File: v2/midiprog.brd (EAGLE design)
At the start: 99.1 x 78.7 mm, 56 parts, among them IC1 PIC18F4550_40, IC2 TPIC6B596N, IC4 TPIC6B596N, Q2 2N2222A, Q3 2N2222A, Q4 2N2222A, Q5 8MHz

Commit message: Removed last via.
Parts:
- moved R5 3.81 mm to (49.5, 39.4)
- moved C8 2.84 mm to (31.8, 45.7)
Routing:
- net VDD: track 286.7 -> 293.5 mm
- net BTN_S0: track 71.1 -> 67.4 mm, vias 1 -> 0
- net SHIFTREG_SCL: track 59.7 -> 62.0 mm
- net N$16: track 15.9 -> 13.8 mm
- net BTN_S3: track 62.3 -> 63.0 mm
- net N$1: track 11.5 -> 12.3 mm
- net BTN_S1: track 68.1 -> 67.4 mm

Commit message: Reorg
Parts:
- moved R5 1.80 mm to (50.8, 40.6)
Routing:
- net VDD: track 293.5 -> 296.9 mm
- net N$17: track 11.5 -> 13.0 mm
- net BTN_IN: track 63.5 -> 64.5 mm
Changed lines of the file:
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@@
 <element name="PWR_CN" library="con-amp-quick" package="02P" value="" x="90.17" y="5.08" rot="R180"/>
 <element name="C9" library="rcl" package="C050-025X075" value=".1" x="7.62" y="44.45" rot="R180"/>
-<element name="R5" library="rcl" package="0207/10" value="10k" x="49.53" y="39.37" rot="R180"/>
+<element name="R5" library="rcl" package="0207/10" value="10k" x="50.8" y="40.64" rot="R180"/>
 <element name="D2" library="diode" package="DO41-10" value="1N4001" x="80.01" y="5.08"/>
 <element name="PWR_SW" library="con-amp-quick" package="02P" value="" x="69.85" y="5.08" rot="R180"/>
@@
 <wire x1="58.42" y1="10.16" x2="58.42" y2="34.29" width="0.4064" layer="1"/>
 <wire x1="58.42" y1="34.29" x2="63.5" y2="34.29" width="0.4064" layer="1"/>
-<wire x1="88.9" y1="29.21" x2="82.55" y2="35.56" width="0.4064" layer="1"/>
-<wire x1="82.55" y1="35.56" x2="78.74" y2="39.37" width="0.4064" layer="1"/>
+<wire x1="88.9" y1="29.21" x2="88.9" y2="31.75" width="0.4064" layer="1"/>
+<wire x1="88.9" y1="31.75" x2="87.63" y2="33.02" width="0.4064" layer="1"/>
+<wire x1="87.63" y1="33.02" x2="83.82" y2="33.02" width="0.4064" layer="1"/>
+<wire x1="83.82" y1="33.02" x2="82.55" y2="34.29" width="0.4064" layer="1"/>
+<wire x1="82.55" y1="34.29" x2="82.55" y2="35.56" width="0.4064" layer="1"/>
+<wire x1="82.55" y1="35.56" x2="82.55" y2="36.83" width="0.4064" layer="1"/>
+<wire x1="82.55" y1="36.83" x2="80.01" y2="39.37" width="0.4064" layer="1"/>
+<wire x1="80.01" y1="39.37" x2="78.74" y2="39.37" width="0.4064" layer="1"/>
 <wire x1="68.58" y1="64.77" x2="67.31" y2="66.04" width="0.4064" layer="1"/>
 <wire x1="67.31" y1="66.04" x2="67.31" y2="68.58" width="0.4064" layer="1"/>
@@
 <wire x1="63.5" y1="74.93" x2="60.96" y2="74.93" width="0.4064" layer="1"/>
 <wire x1="57.15" y1="74.93" x2="60.96" y2="74.93" width="0.4064" layer="1"/>
-<wire x1="44.45" y1="39.37" x2="48.26" y2="35.56" width="0.4064" layer="1"/>
+<wire x1="45.72" y1="40.64" x2="45.72" y2="38.1" width="0.4064" layer="1"/>
+<wire x1="45.72" y1="38.1" x2="48.26" y2="35.56" width="0.4064" layer="1"/>
 <wire x1="58.42" y1="35.56" x2="48.26" y2="35.56" width="0.4064" layer="1"/>
 <wire x1="58.42" y1="34.29" x2="58.42" y2="35.56" width="0.4064" layer="1"/>
@@
 <wire x1="10.16" y1="38.1" x2="16.51" y2="31.75" width="0.4064" layer="1"/>
 <wire x1="10.16" y1="44.45" x2="10.16" y2="38.1" width="0.4064" layer="1"/>
-<wire x1="68.58" y1="49.53" x2="78.74" y2="39.37" width="0.4064" layer="1"/>
-<wire x1="68.58" y1="64.77" x2="68.58" y2="49.53" width="0.4064" layer="1"/>
+<wire x1="68.58" y1="46.99" x2="76.2" y2="39.37" width="0.4064" layer="1"/>
+<wire x1="76.2" y1="39.37" x2="78.74" y2="39.37" width="0.4064" layer="1"/>
+<wire x1="68.58" y1="64.77" x2="68.58" y2="46.99" width="0.4064" layer="1"/>
 <wire x1="10.16" y1="44.45" x2="33.02" y2="44.45" width="0.4064" layer="1"/>
 <wire x1="33.02" y1="44.45" x2="34.29" y2="45.72" width="0.4064" layer="1"/>
 <wire x1="49.53" y1="44.45" x2="49.53" y2="49.53" width="0.4064" layer="16"/>
-<wire x1="44.45" y1="39.37" x2="49.53" y2="44.45" width="0.4064" layer="16"/>
+<wire x1="45.72" y1="40.64" x2="49.53" y2="44.45" width="0.4064" layer="16"/>
 <wire x1="20.32" y1="49.53" x2="20.32" y2="48.26" width="0.4064" layer="1"/>
 <wire x1="20.32" y1="48.26" x2="19.05" y2="46.99" width="0.4064" layer="1"/>
@@
 <contactref element="R5" pad="1"/>
 <contactref element="U$2" pad="3"/>
-<wire x1="63.5" y1="39.37" x2="54.61" y2="39.37" width="0.254" layer="1"/>
-<wire x1="50.8" y1="39.37" x2="54.61" y2="39.37" width="0.254" layer="16"/>
-<wire x1="41.91" y1="36.83" x2="48.26" y2="36.83" width="0.254" layer="16"/>
-<wire x1="48.26" y1="36.83" x2="50.8" y2="39.37" width="0.254" layer="16"/>
-<wire x1="34.29" y1="29.21" x2="41.91" y2="36.83" width="0.254" layer="16"/>
+<wire x1="63.5" y1="39.37" x2="57.15" y2="39.37" width="0.254" layer="1"/>
+<wire x1="57.15" y1="39.37" x2="55.88" y2="40.64" width="0.254" layer="1"/>
+<wire x1="52.07" y1="40.64" x2="55.88" y2="40.64" width="0.254" layer="16"/>
+<wire x1="43.18" y1="38.1" x2="49.53" y2="38.1" width="0.254" layer="16"/>
+<wire x1="49.53" y1="38.1" x2="52.07" y2="40.64" width="0.254" layer="16"/>
+<wire x1="34.29" y1="29.21" x2="43.18" y2="38.1" width="0.254" layer="16"/>
 <wire x1="34.29" y1="26.67" x2="34.29" y2="29.21" width="0.254" layer="16"/>
 <wire x1="31.75" y1="24.13" x2="34.29" y2="26.67" width="0.254" layer="16"/>
@@
 <contactref element="IC1" pad="40"/>
 <contactref element="ICD" pad="4"/>
-<wire x1="72.39" y1="68.58" x2="72.39" y2="66.04" width="0.4064" layer="1"/>
-<wire x1="72.39" y1="66.04" x2="78.74" y2="59.69" width="0.4064" layer="1"/>
+<wire x1="72.39" y1="68.58" x2="72.39" y2="63.5" width="0.4064" layer="1"/>
+<wire x1="72.39" y1="63.5" x2="76.2" y2="59.69" width="0.4064" layer="1"/>
+<wire x1="76.2" y1="59.69" x2="78.74" y2="59.69" width="0.4064" layer="1"/>
 </signal>
 <signal name="N$18">

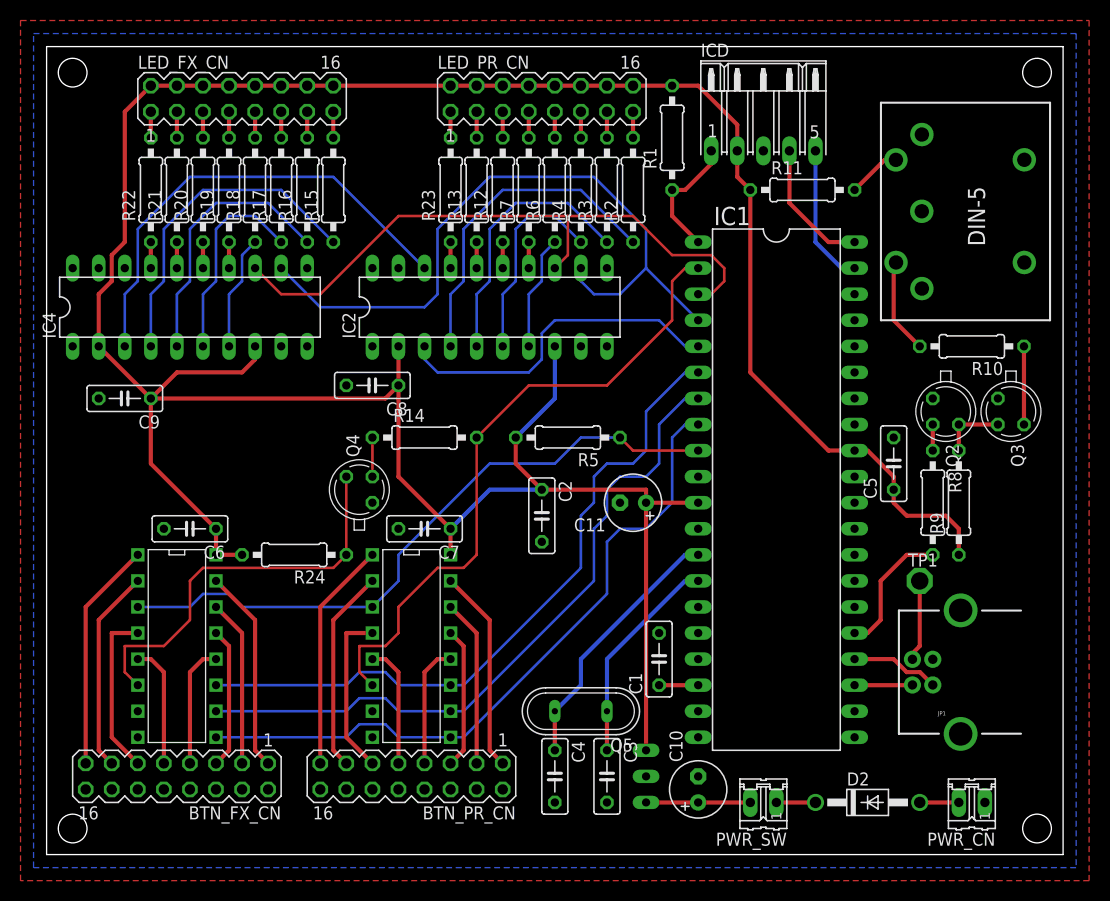
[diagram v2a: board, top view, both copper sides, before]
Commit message: More clearance between button headers and mux chips. Moved timing crystal closer to PIC. Swapped C11 and C2 positions. Swapped MIDI OUT pins.
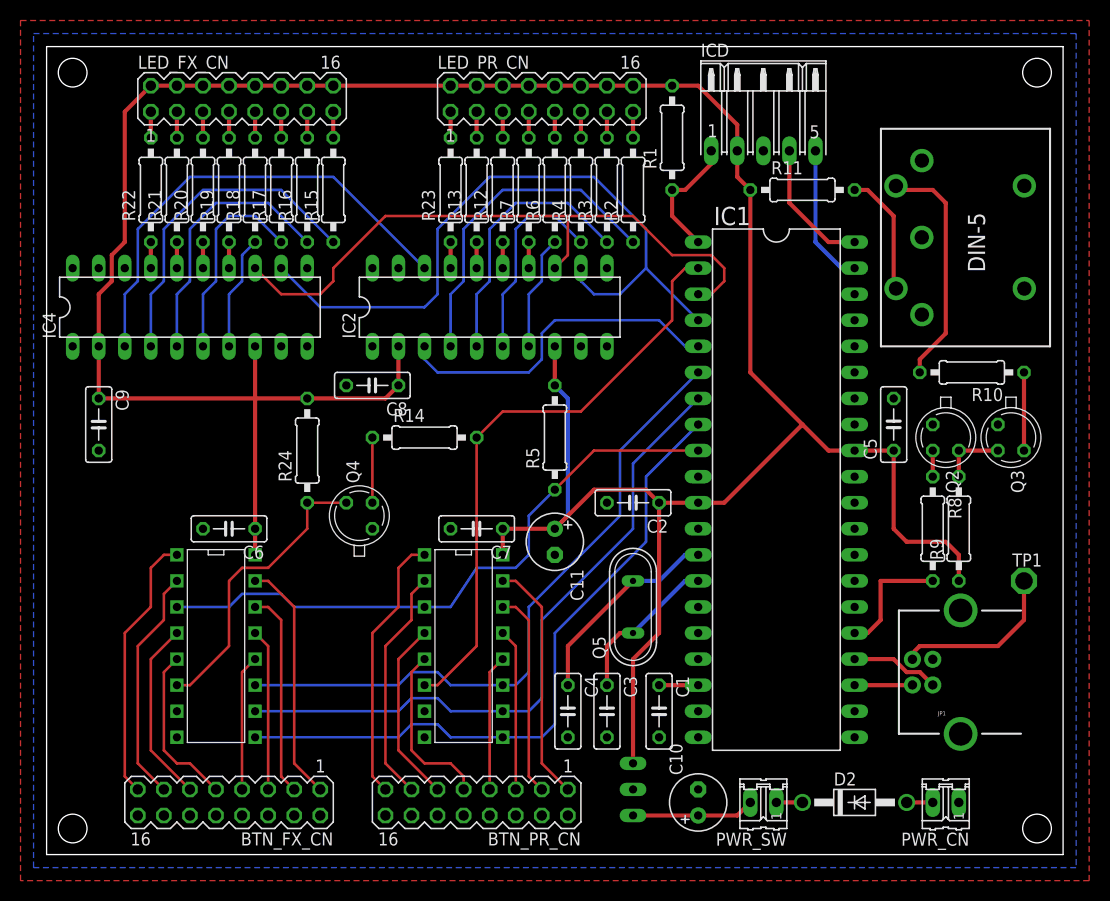
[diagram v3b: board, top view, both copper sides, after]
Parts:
- moved Q5 11.4 mm to (57.1, 24.1), turned to 90 degrees
- moved R24 10.2 mm to (25.4, 39.4), turned to 90 degrees
- moved TP1 10.2 mm to (95.2, 26.7)
- moved C2 8.98 mm to (57.1, 34.3), turned to 180 degrees
- moved C11 8.52 mm to (49.5, 30.5), turned to 270 degrees
- moved BTN_PR_CN 6.84 mm to (41.9, 5.08)
- moved C4 6.48 mm to (50.8, 14.0)
- moved C3 6.35 mm to (54.6, 14.0)
- moved BTN_FX_CN 5.68 mm to (17.8, 5.08)
- moved U$1 5.08 mm to (44.5, 19.1)
- moved C1 5.08 mm to (59.7, 14.0), turned to 270 degrees
- moved C7 5.08 mm to (41.9, 31.8)
- moved C6 3.81 mm to (17.8, 31.8)
- moved U$2 3.81 mm to (20.3, 19.1)
- moved C5 3.81 mm to (82.5, 41.9)
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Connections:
- net N$8: now also R11.2; no longer R10.2
- net N$9: now also R10.2; no longer R11.2
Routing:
- net N$9: track 5.24 -> 23.1 mm
- net N$54: track 39.5 -> 29.1 mm
- net VDD: track 296.9 -> 286.8 mm
- net USB_VCC: track 7.93 -> 16.6 mm
- net OSC2: track 20.9 -> 15.3 mm
- net OSC1: track 25.6 -> 20.2 mm
- net BTN_S3: track 63.0 -> 57.6 mm
- net N$47: track 12.0 -> 16.8 mm
- net N$46: track 12.0 -> 16.1 mm
- net N$64: track 19.9 -> 23.7 mm
- net N$52: track 22.4 -> 26.2 mm
- net N$63: track 16.3 -> 20.1 mm
- net N$60: track 22.4 -> 26.2 mm
- net N$57: track 16.3 -> 20.1 mm
- net N$58: track 19.9 -> 23.7 mm
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
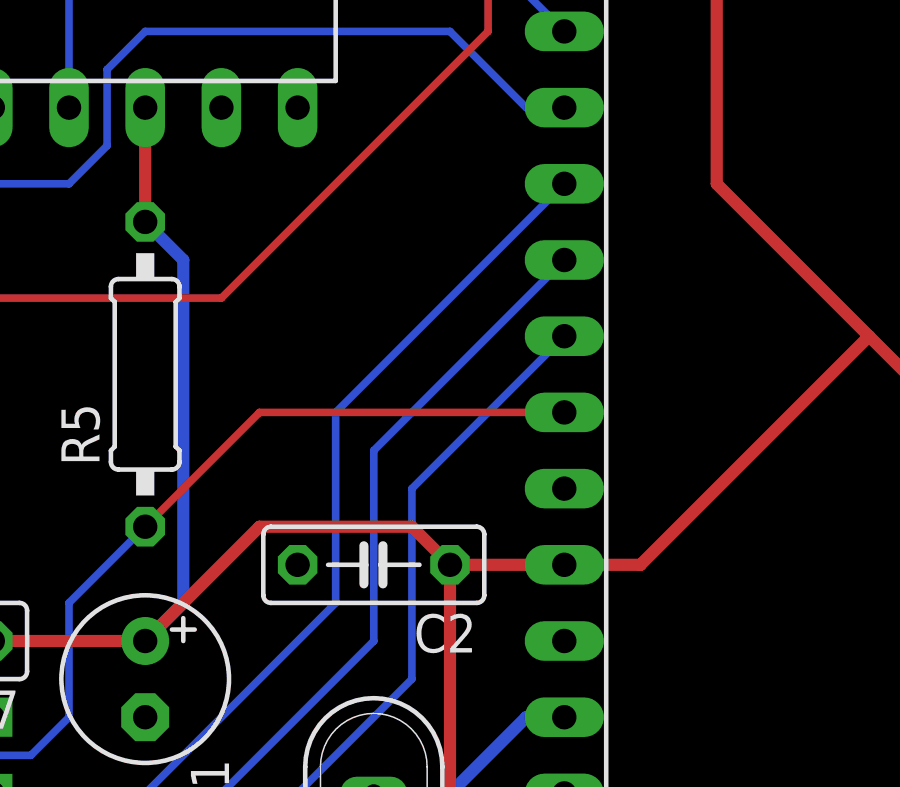
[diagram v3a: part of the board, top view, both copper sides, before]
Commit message: Fixed missing chunk of bottom ground plane.
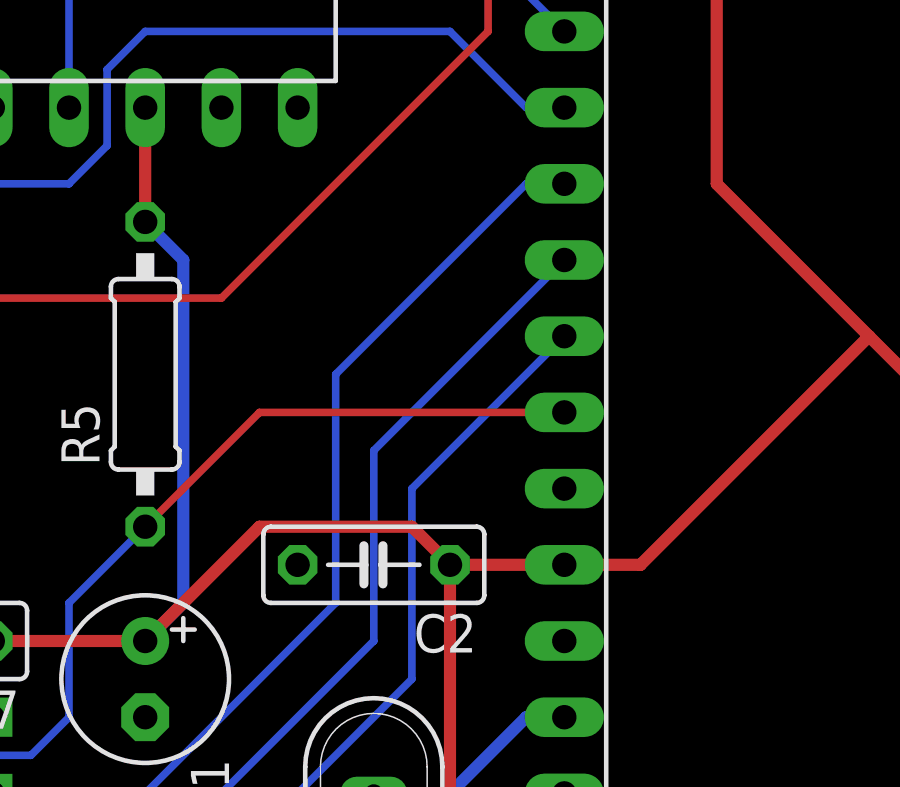
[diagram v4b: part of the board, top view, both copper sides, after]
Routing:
- net BTN_S0: track 64.3 -> 65.0 mm
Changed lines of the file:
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@@
 <contactref element="U$2" pad="11"/>
 <contactref element="U$1" pad="11"/>
-<wire x1="63.5" y1="46.99" x2="55.88" y2="39.37" width="0.254" layer="16"/>
-<wire x1="55.88" y1="39.37" x2="55.88" y2="33.02" width="0.254" layer="16"/>
+<wire x1="63.5" y1="46.99" x2="62.23" y2="46.99" width="0.254" layer="16"/>
+<wire x1="62.23" y1="46.99" x2="55.88" y2="40.64" width="0.254" layer="16"/>
+<wire x1="55.88" y1="40.64" x2="55.88" y2="33.02" width="0.254" layer="16"/>
 <wire x1="55.88" y1="33.02" x2="46.99" y2="24.13" width="0.254" layer="16"/>
 <wire x1="46.99" y1="24.13" x2="46.99" y2="17.78" width="0.254" layer="16"/>

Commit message: Holy boards, batman!
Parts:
- moved TP1 1.27 mm to (95.2, 25.4)
- moved JP1 1.27 mm to (86.4, 16.5)
- moved C8 1.27 mm to (31.8, 44.5)
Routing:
- net VDD: track 286.8 -> 289.7 mm
- net MIDI_TX: track 12.0 -> 10.5 mm
- net USB_VCC: track 16.6 -> 17.7 mm
- net N$31: track 45.7 -> 46.4 mm
- net N$47: track 16.8 -> 16.1 mm
- net USB_D-: track 5.65 -> 6.17 mm
- net USB_D+: track 8.66 -> 9.19 mm
